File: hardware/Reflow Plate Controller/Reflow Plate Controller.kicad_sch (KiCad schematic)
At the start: 86 parts, among them J1 SWD, J2 USB_C_Receptacle_USB2.0_16P, J3 JST-XH, J4 OLED, J5 XT30, J6 XT30, Q1 AO4262E, Q2 SUD50P06-15, Q3 BSS138, SW1 SW_SPST, SW2 SW_SPST, SW3 SW_SPST, SW4 SW_SPST, SW5 SW_SPST, SW6 SW_SPST, SW7 SW_SPST, U1 L78L12ABU, U2 TPS560430, U3 STM32G431KBTx, U4 D5V0P4UR6SO-7, U5 TPD6S300A, U6 UCC27511ADBV

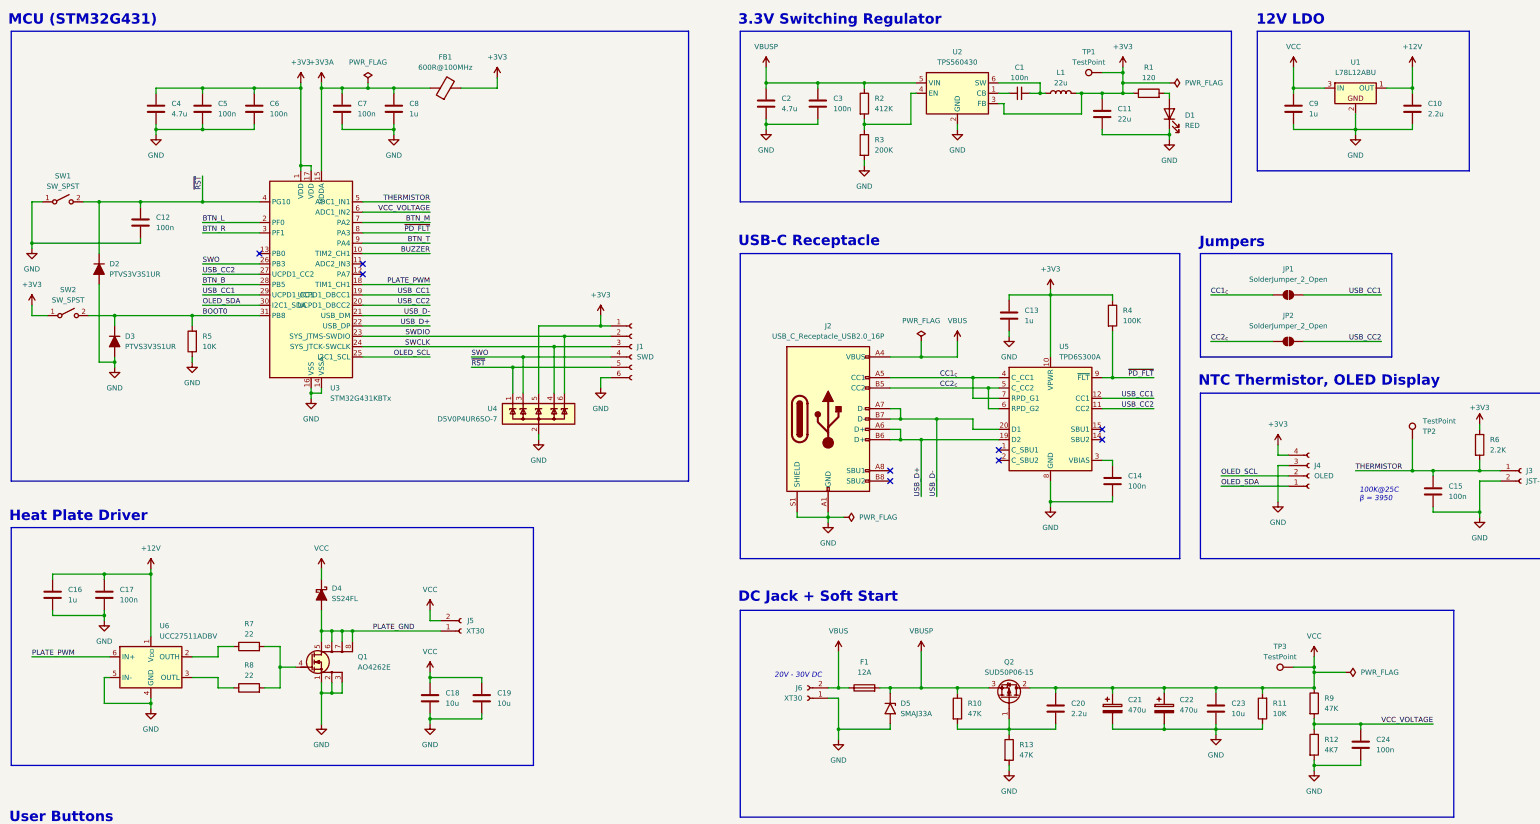
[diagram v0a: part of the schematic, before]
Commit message: Fix a few layout and component selection issues
- Replace out-of-stock components
- Remove some of the 100nF caps that are in parallel with a larger value
- Swap PTVS3V3 -> SD03
- Swap the PMOS to HSU6119 and the NMOS to DOD130N06 for lower Rds(on)
- Slightly increase the copper area around the FETs
- Reduce the soft-start duration to 47 ms
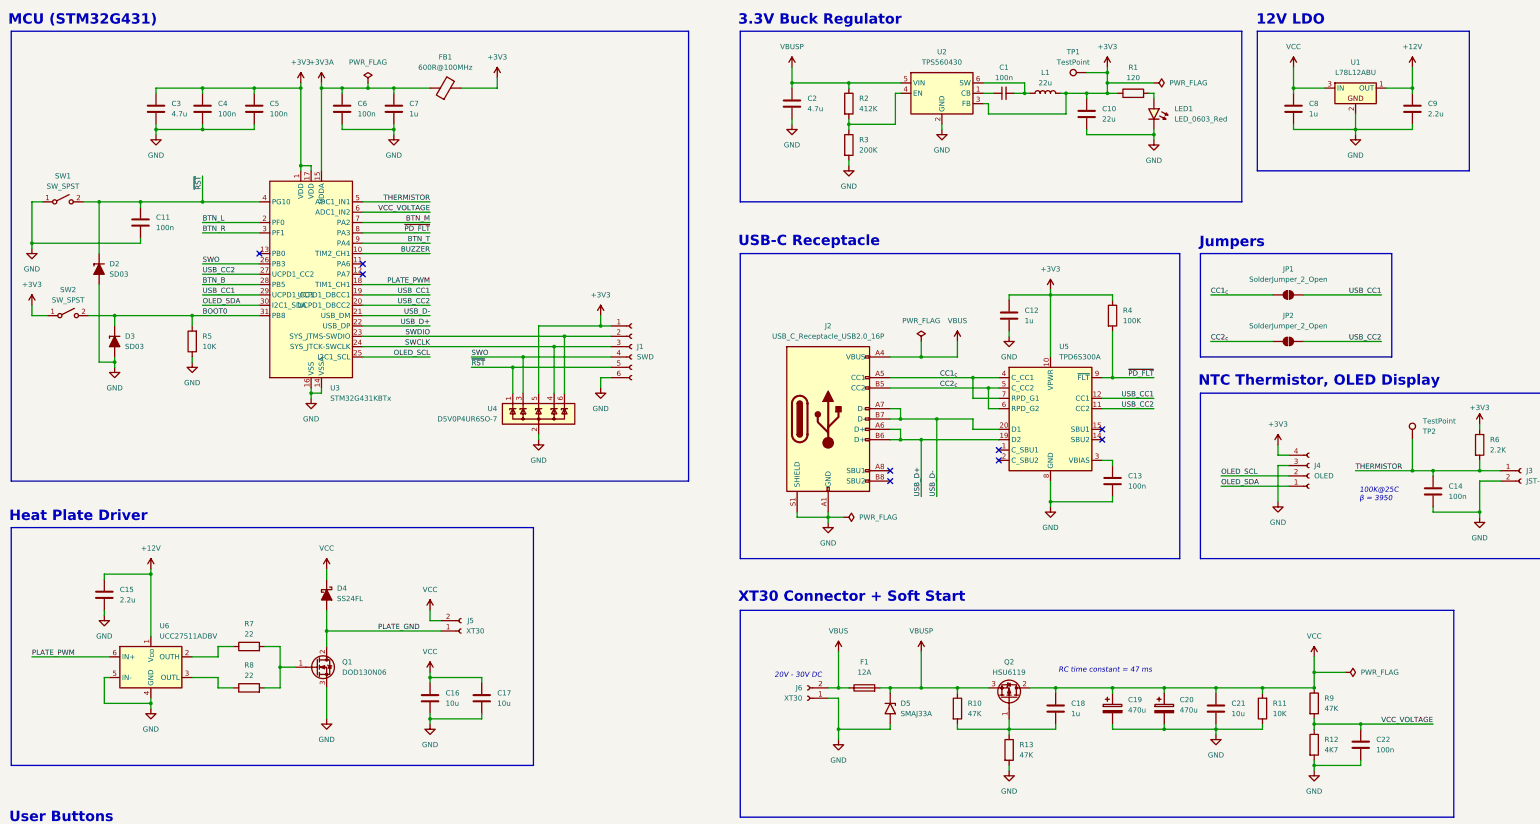
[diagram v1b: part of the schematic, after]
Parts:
- removed C16: 1u, Capacitor_SMD:C_0805_2012Metric_Pad1.18x1.45mm_HandSolder, symbol Device:C
- removed C17, C3: 100n, Capacitor_SMD:C_0603_1608Metric_Pad1.08x0.95mm_HandSolder, symbol Device:C
- removed D1: RED, LED_SMD:LED_0805_2012Metric_Pad1.15x1.40mm_HandSolder, symbol Device:LED
- removed D2, D3: PTVS3V3S1UR, Diode_SMD:Nexperia_CFP3_SOD-123W, symbol Diode_TVS:PTVS3V3S1UR
- removed Q1: AO4262E, PCM_Package_SO_AKL:SO-8_3.9x4.9mm_P1.27mm, symbol PCM_Transistor_MOSFET_AKL:AO4262E
- removed Q2: SUD50P06-15, Package_TO_SOT_SMD:TO-252-2, symbol Transistor_FET:SUD50P06-15
- removed TP3: TestPoint, TestPoint:TestPoint_Pad_D1.0mm, symbol Connector:TestPoint
- added C15: 2.2u, Capacitor_SMD:C_0805_2012Metric_Pad1.18x1.45mm_HandSolder, symbol Device:C
- added D2, D3: SD03, PCM_Diode_SMD_AKL:D_SOD-323_HandSoldering, symbol Diode_TVS:SD03
- added LED1: LED_0603_Red, PCM_LED_SMD_AKL:LED_0603_1608Metric, symbol PCM_LED_AKL:LED_0603_Red
- added Q1: DOD130N06, Package_TO_SOT_SMD:TO-252-2, symbol Transistor_FET_Custom:DOD130N06
- added Q2: HSU6119, Package_TO_SOT_SMD:TO-252-2, symbol Transistor_FET_Custom:HSU6119
- C18: renamed from C20; value 2.2u -> 1u
- D4: footprint PCM_Diode_SMD_AKL:D_SOD-123F -> PCM_Diode_SMD_Handsoldering_AKL:D_SOD-123F
- renumbered C11 to C10, C12 to C11, C13 to C12, C14 to C13, C15 to C14, C18 to C16, C19 to C17, C21 to C19, C22 to C20, C23 to C21, C24 to C22, C4 to C3, C5 to C4, C6 to C5, C7 to C6, C8 to C7, C9 to C8, C10 to C9
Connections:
- net +12V: now also C15.1
- net BOOT0: now also D3.1
- net GND: now also C15.2, D2.2, D3.2, LED1.1 (K), Q1.3 (S)
- net PLATE_GND: now also Q1.2 (D)
- net VBUSP: now also Q2.3 (S)
- net VCC: now also Q2.2 (D)
- net ~{RST}: now also D2.1
- net at C18.2, R10.2, R13.1: now also Q2.1 (G)
- net at R1.2: now also LED1.2 (A)
- net at R7.2, R8.2: now also Q1.1 (G)
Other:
- note added: "3.3V Buck Regulator"
- note added: "RC time constant = 47 ms"
- note added: "XT30 Connector + Soft Start"
- note removed: "3.3V Switching Regulator"
- note removed: "DC Jack + Soft Start"
- moved on the sheet: C1, C10, C2, D4, L1, R1, R2, R3, TP1, U2
